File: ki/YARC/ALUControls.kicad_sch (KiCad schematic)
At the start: 0 parts

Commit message: Believable ALU/Flags design almost complete
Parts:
- added U?: 74LS574, symbol 74xx:74LS574
- added U? (x5): 74LS00, symbol 74xx:74LS00
- added U? (x5): 74LS32, symbol 74xx:74LS32
- added U? (x10): 74LS08, symbol 74xx:74LS08
- added U? (x3): 74LS74, symbol 74xx:74LS74
- added U?: 74LS157, symbol 74xx:74LS157
- added U?: 74LS245, symbol 74xx:74LS245
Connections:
- new net: U?.20 (VCC), U?.6 (D4), U?.7 (D5), U?.8 (D6), U?.9 (D7)
- new net: U?.13, U?.6
- new net: U?.12, U?.9 (Q)
- new net: U?.2 (D), U?.3, U?.5
- new net: U?.4, U?.5 (Q)
- new net: U?.3, U?.5
- new net: U?.11, U?.4
- new net ALU_PHI_2: U?.1
- new net CARRY_IN: U?.6
- new net FHALF.C: U?.12 (D)
- new net FHALF.Z: U?.2
- new net FMUX.C: U?.2 (D0), U?.4 (Za)
- new net FMUX.N: U?.4 (D2), U?.9 (Zc)
- new net FMUX.V: U?.12 (Zd), U?.5 (D3)
- new net FMUX.Z: U?.3 (D1), U?.7 (Zb)
- new net FMUXIN.C: U?.2 (I0a)
- new net FMUXIN.N: U?.11 (I0c)
- new net FMUXIN.V: U?.14 (I0d)
- new net FMUXIN_Z: U?.5 (I0b), U?.6
- new net FQTR.C: U?.1, U?.10, U?.2, U?.9
- new net FQTR.Z: U?.1
- new net FREG.C: U?.19 (Q0), U?.2, U?.2 (A0)
- new net FREG.N: U?.17 (Q2), U?.4 (A2)
- new net FREG.V: U?.16 (Q3), U?.5 (A3)
- new net FREG.Z: U?.18 (Q1), U?.3 (A1)
- new net GND: U?.1 (OE), U?.10, U?.10, U?.10, U?.10 (GND), U?.10 (GND), U?.12, U?.12, U?.13, U?.13, U?.15 (E), U?.4, U?.5, U?.6 (A4), U?.7 (A5), U?.7 (GND), U?.7 (GND), U?.7 (GND), U?.7 (GND), U?.7 (GND), U?.8 (A6), U?.8 (GND), U?.9, U?.9, U?.9, U?.9 (A7)
- new net K16: U?.12
- new net K2: U?.1 (S)
- new net K3: U?.1
- new net LD_FLGS_CLK: U?.11, U?.11 (Cp)
- new net PHI_1_CLK: U?.11 (C), U?.3 (C)
- new net PHI_2_CLK: U?.3, U?.4, U?.5
- new net SYSCLK: U?.13, U?.2
- new net SYSDATA0: U?.18 (B0), U?.3 (I1a)
- new net SYSDATA1: U?.17 (B1), U?.6 (I1b)
- new net SYSDATA2: U?.10 (I1c), U?.16 (B2)
- new net SYSDATA3: U?.13 (I1d), U?.15 (B3)
- new net VCC: U?.1 (A->B), U?.1 (~{R}), U?.10 (~{S}), U?.13 (~{R}), U?.14 (VCC), U?.14 (VCC), U?.14 (VCC), U?.14 (VCC), U?.14 (VCC), U?.16 (VCC), U?.20 (VCC), U?.4 (~{S})
- new net ~{FQTR_C}: U?.3
- new net ~{FQTR_NOT_C}: U?.8
- new net ~{SYSDATA_SRC_IS_F}: U?.19 (CE)
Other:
- note added: "CARRY-IN LOGIC"
- note added: "CARRY-SELECT CONTROLS"
- note added: "SPARES"
- note added: "ZERO DETECTOR"

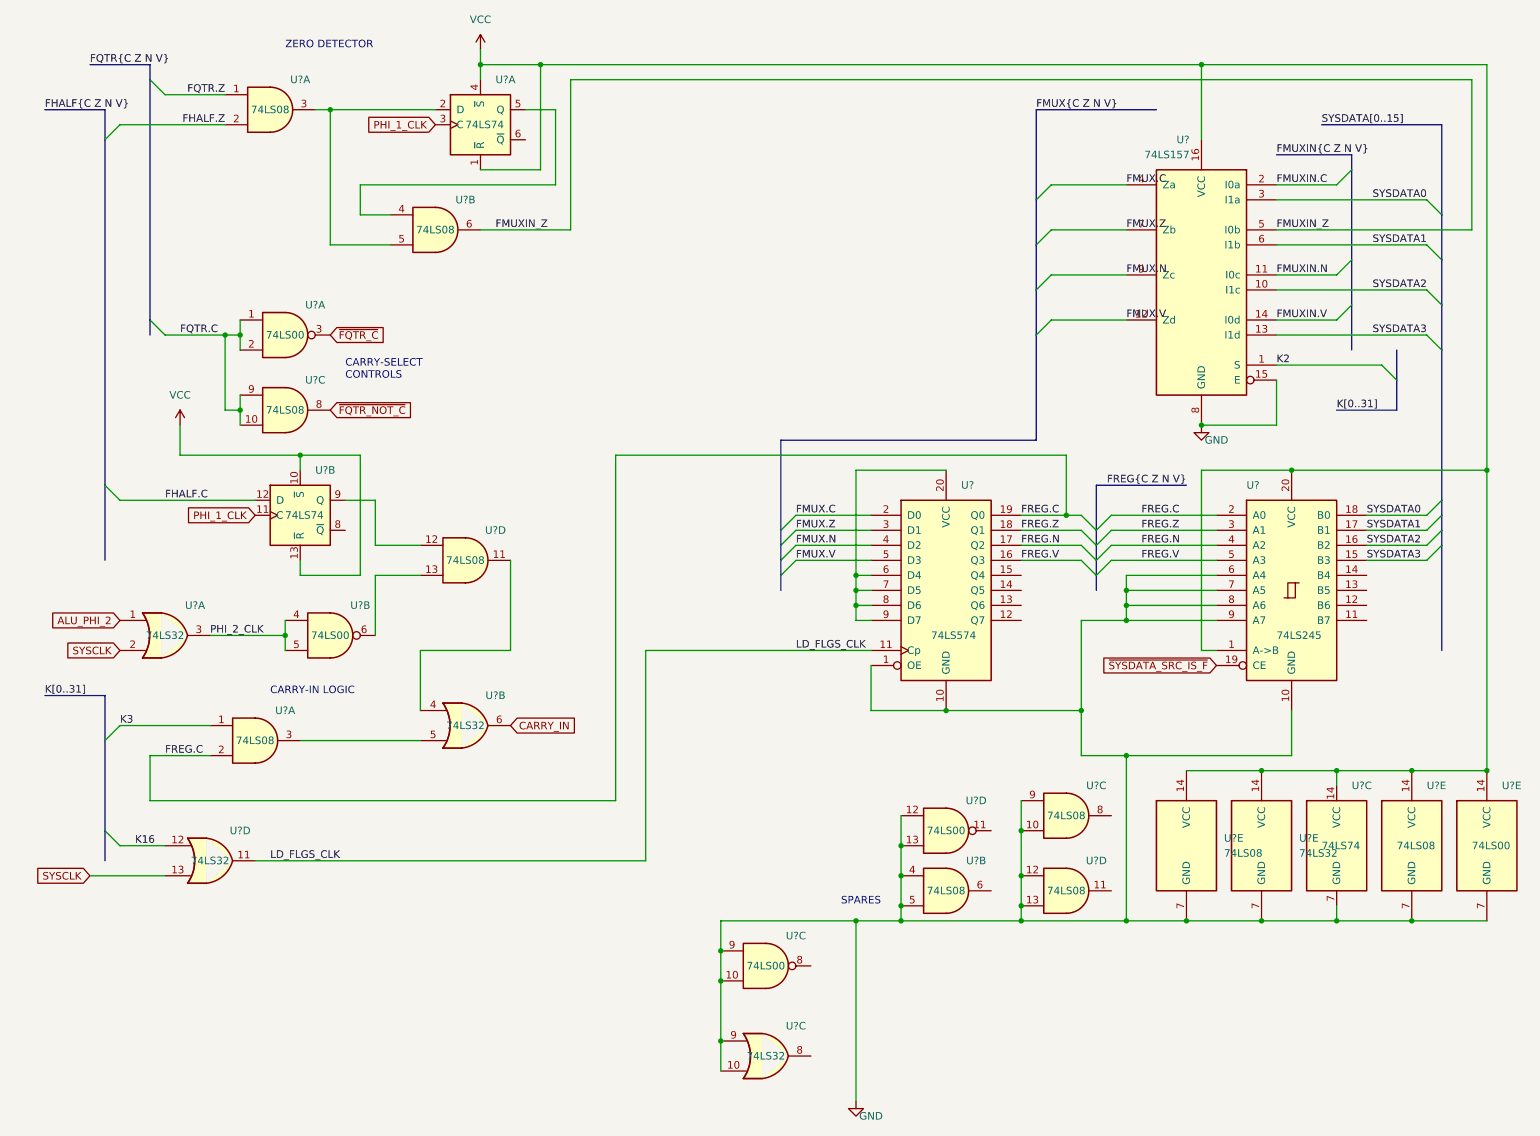
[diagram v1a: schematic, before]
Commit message: Further development of ALU controls
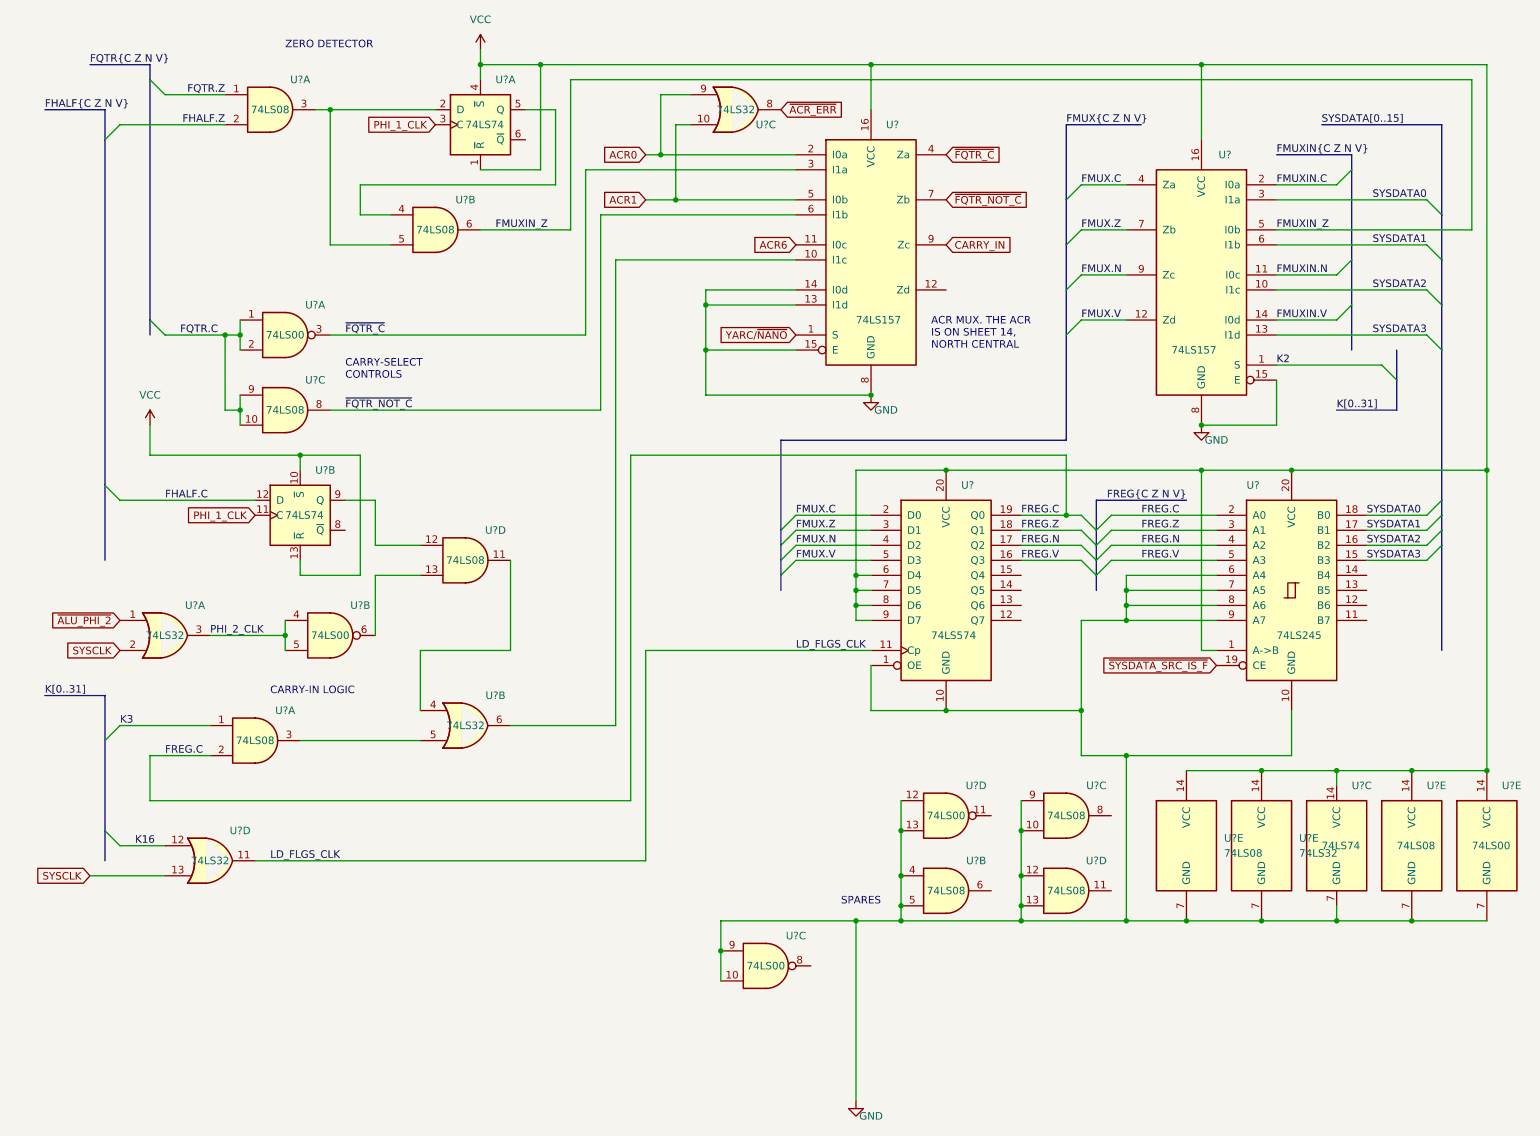
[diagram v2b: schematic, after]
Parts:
- added U?: 74LS157, symbol 74xx:74LS157
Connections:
- net CARRY_IN: now also U?.9 (Zc); no longer U?.6
- net GND: now also U?.13 (I1d), U?.14 (I0d), U?.15 (E), U?.8 (GND); no longer U?.10, U?.9
- net VCC: now also U?.20 (VCC), U?.6 (D4), U?.7 (D5), U?.8 (D6), U?.9 (D7), U?.16 (VCC)
- net ~{FQTR_C}: now also U?.3 (I1a), U?.4 (Za)
- net ~{FQTR_NOT_C}: now also U?.6 (I1b), U?.7 (Zb)
- net ~{ACR_ERR}: now reaches U?.8
- net ALU_PHI_2 renamed ~{ALU_PHI_2}
- new net: U?.10 (I1c), U?.6
- new net ACR0: U?.2 (I0a), U?.9
- new net ACR1: U?.10, U?.5 (I0b)
- new net ACR6: U?.11 (I0c)
- new net YARC/~{NANO}: U?.1 (S)
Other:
- note added: "ACR MUX. THE ACR IS ON SHEET 14, NORTH CENTRAL"
- moved on the sheet: U?C, U?D

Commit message: ALU schematic checking complete. Ready to start layout.
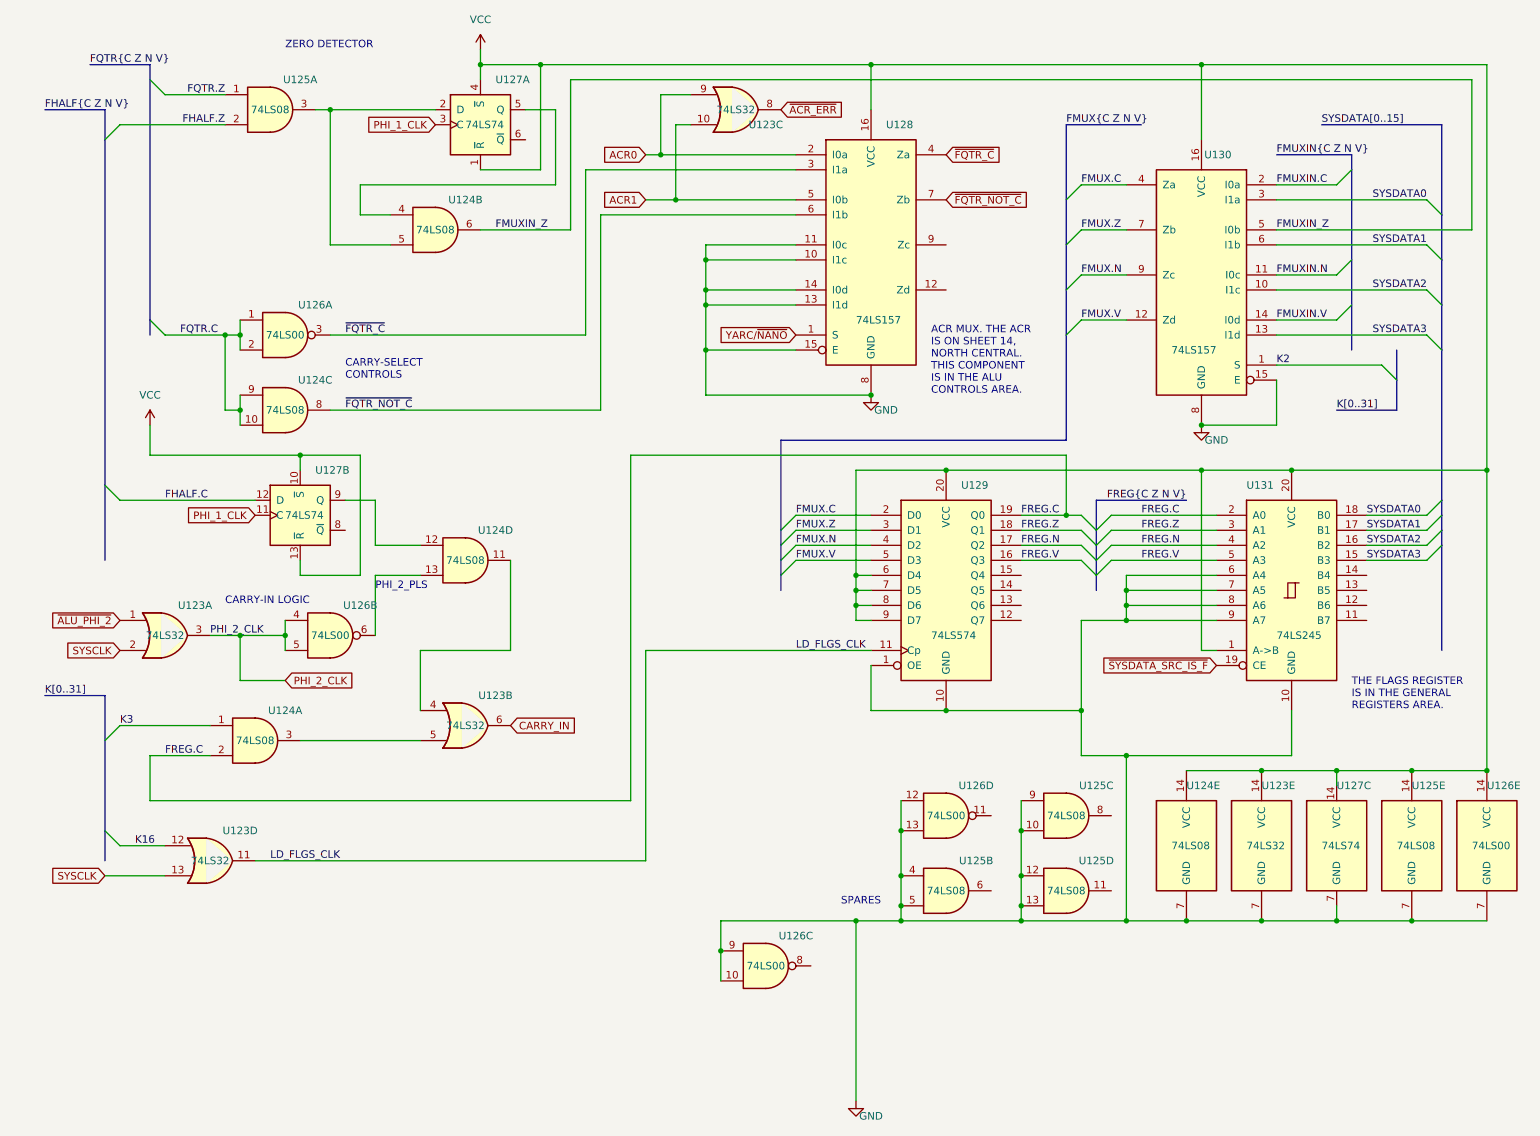
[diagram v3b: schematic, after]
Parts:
- gave numbers to parts that had none: 9
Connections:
- net ACR6 is gone; now on net GND: U128.11 (I0c)
- net CARRY_IN: now also U123.6; no longer U128.9 (Zc)
- net GND: now also U128.10 (I1c)
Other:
- note added: "ACR MUX. THE ACR IS ON SHEET 14, NORTH CENTRAL. THIS COMPONENT IS IN THE ALU CONTROLS AREA."
- note added: "PHI_2_PLS"
- note added: "THE FLAGS REGISTER IS IN THE GENERAL REGISTERS AREA."
- note removed: "ACR MUX. THE ACR IS ON SHEET 14, NORTH CENTRAL"

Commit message: Improvements to ALU and Flags schematic. Begin work on layout.
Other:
- note added: "U130 AND U131 ARE IN THE GENERAL REGISTERS AREA."
- note removed: "THE FLAGS REGISTER IS IN THE GENERAL REGISTERS AREA."
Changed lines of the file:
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@@
     (stroke (width 0) (type default) (color 0 0 0 0))
   )
-  (text "THE FLAGS REGISTER\nIS IN THE GENERAL\nREGISTERS AREA."
-    (at 236.22 132.08 0)
+  (text "U130 AND U131 ARE\nIN THE GENERAL\nREGISTERS AREA." (at 236.22 132.08 0)
     (effects (font (size 1.27 1.27)) (justify left bottom))
   )
@@
   (symbol (lib_id "74xx:74LS157") (at 210.82 58.42 0) (mirror y) (unit 1)
     (in_bom yes) (on_board yes)
-    (property "Reference" "U130" (id 0) (at 215.9 38.1 0)
-      (effects (font (size 1.27 1.27)) (justify left))
-    )
+    (property "Reference" "U130" (id 0) (at 208.28 38.1 0)
+      (effects (font (size 1.27 1.27)) (justify left))
+    )

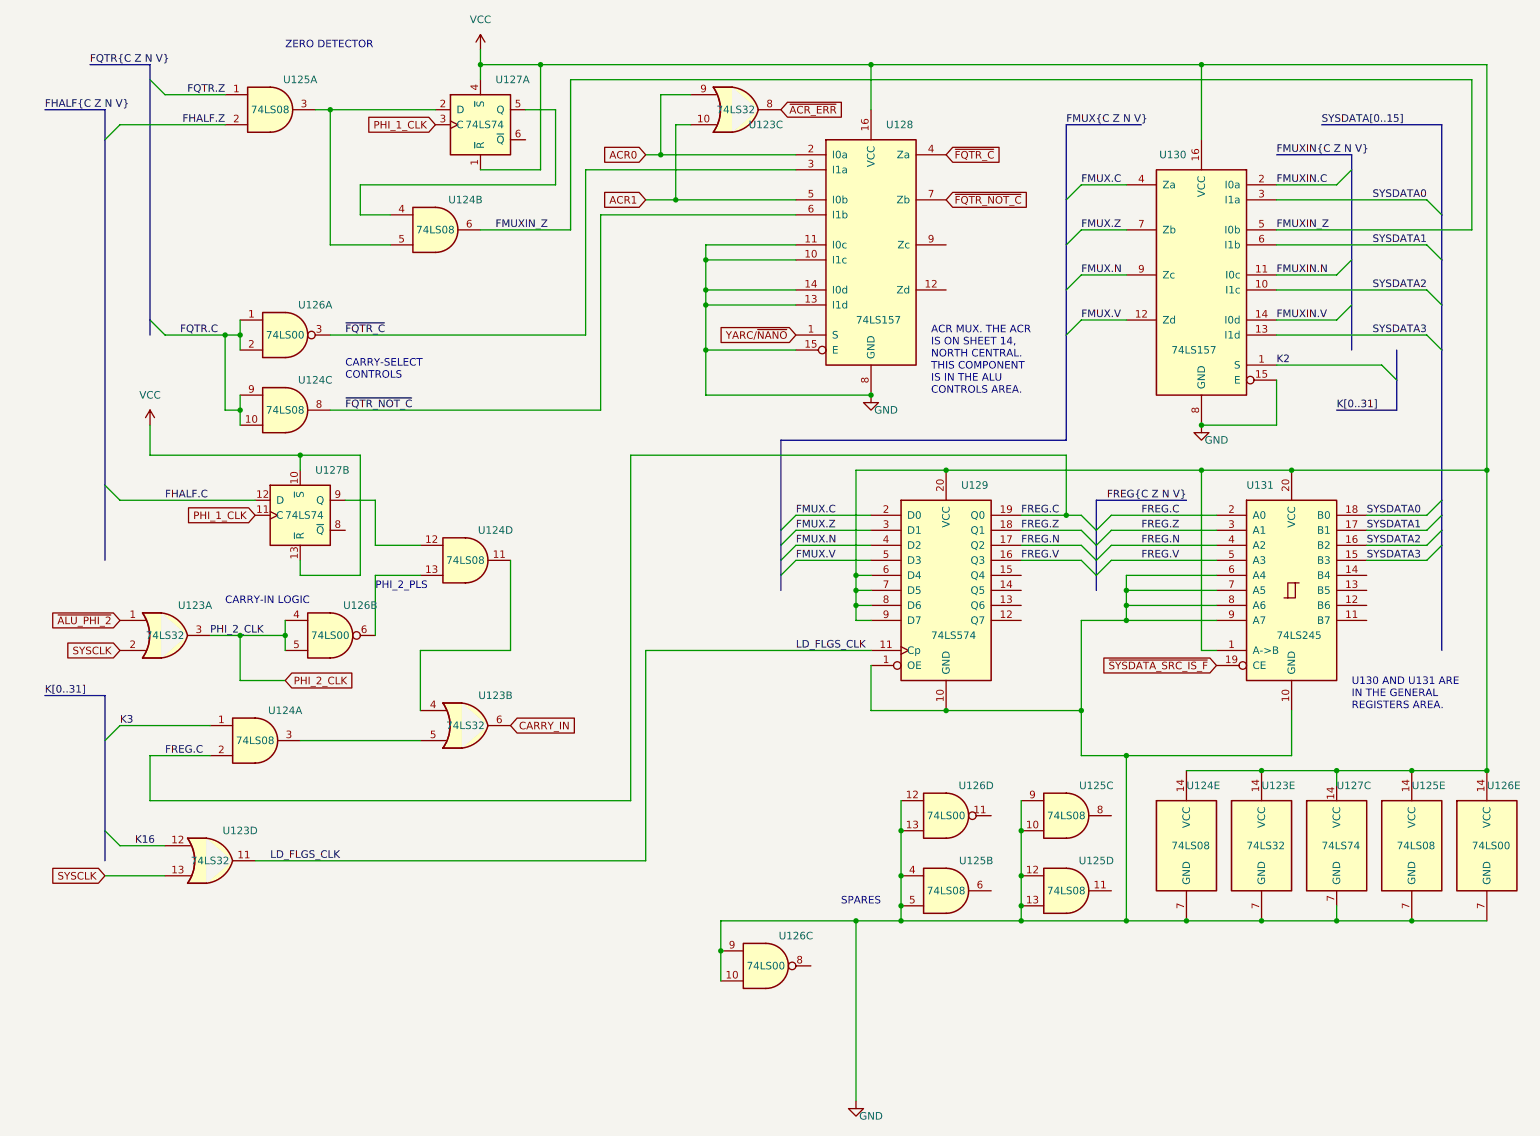
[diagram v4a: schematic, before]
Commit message: Ongoing development of ALU and Flags. Construction start.
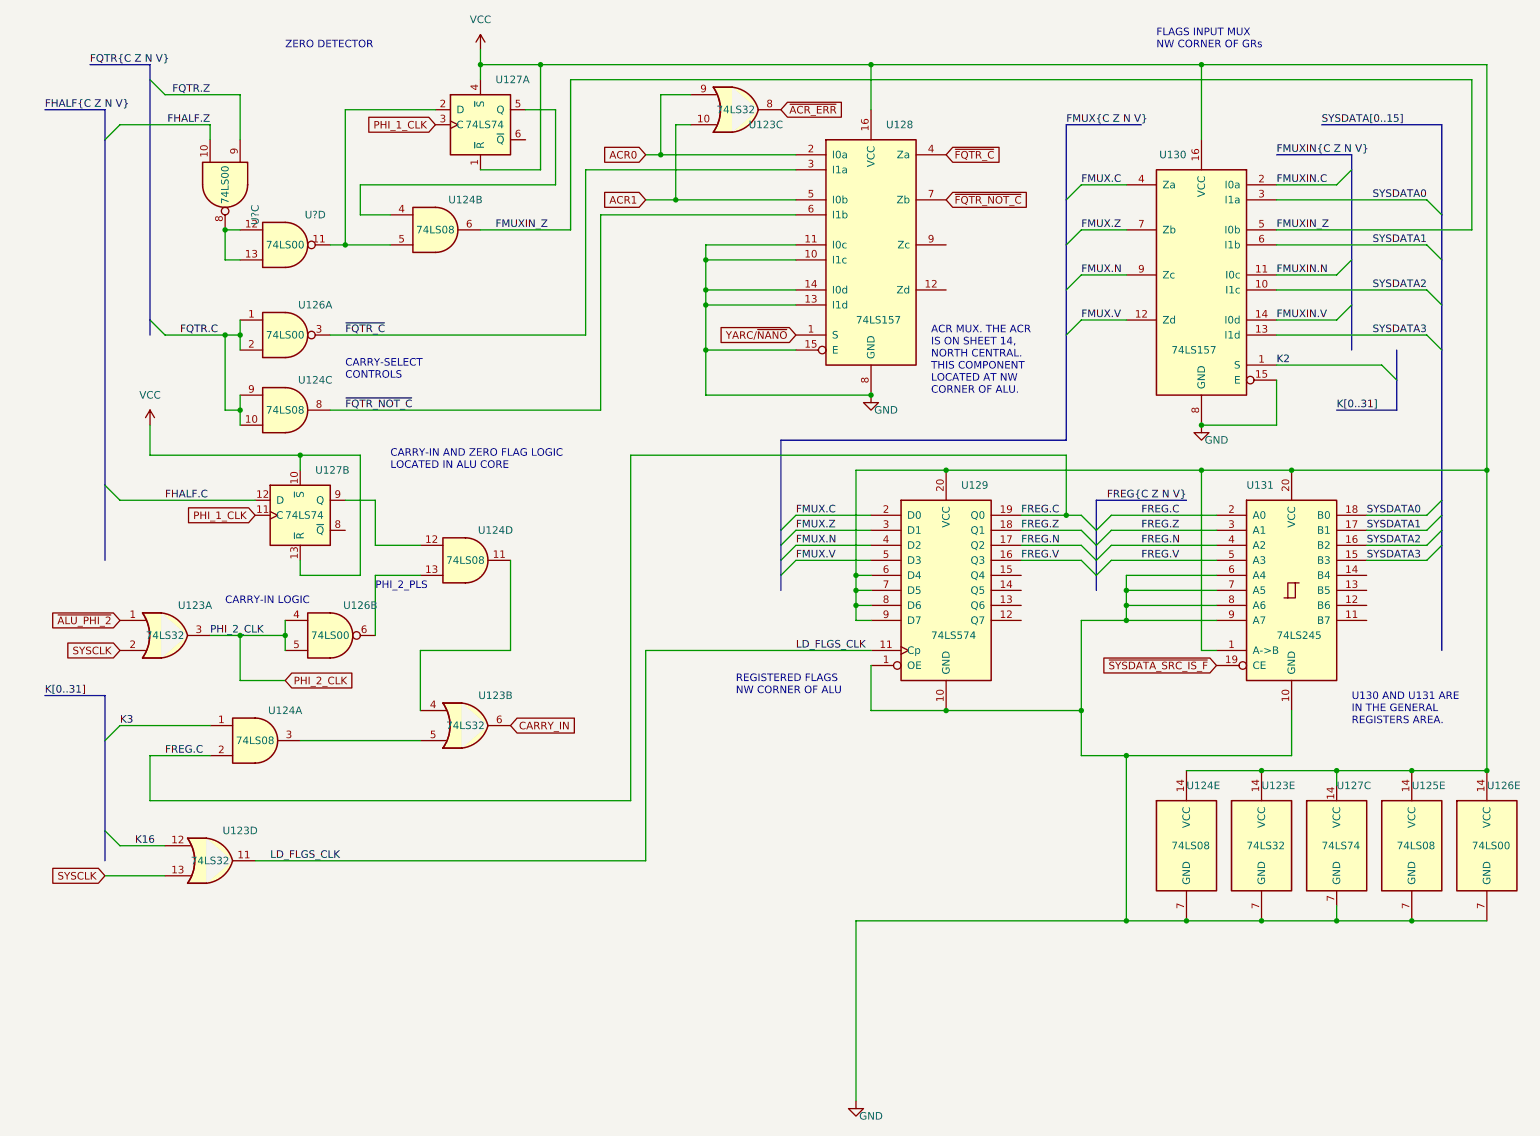
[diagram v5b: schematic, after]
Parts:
- removed unit 4 of U125
- removed unit 1 of U125
- removed unit 3 of U125
- removed unit 2 of U125
- removed unit 4 of U126
- removed unit 3 of U126
- added U? (x2): 74LS00, symbol 74xx:74LS00
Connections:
- net FHALF.Z: now also U?.10
- net FQTR.Z: now also U?.9
- net at U124.5, U127.2 (D): now also U?.11
- new net: U?.12, U?.13, U?.8
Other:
- note added: "ACR MUX. THE ACR IS ON SHEET 14, NORTH CENTRAL. THIS COMPONENT LOCATED AT NW CORNER OF ALU."
- note added: "CARRY-IN AND ZERO FLAG LOGIC LOCATED IN ALU CORE"
- note added: "FLAGS INPUT MUX NW CORNER OF GRs"
- note added: "REGISTERED FLAGS NW CORNER OF ALU"
- note removed: "ACR MUX. THE ACR IS ON SHEET 14, NORTH CENTRAL. THIS COMPONENT IS IN THE ALU CONTROLS AREA."
- note removed: "SPARES"
